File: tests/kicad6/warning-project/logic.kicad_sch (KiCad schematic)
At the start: 2 parts

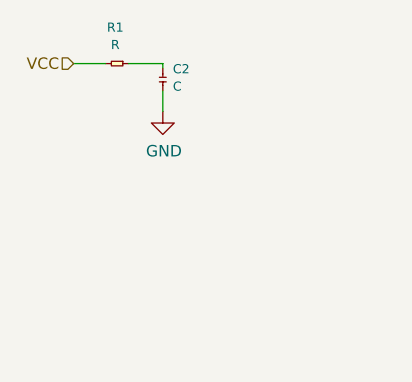
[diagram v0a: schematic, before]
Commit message: Changed the "warning" KiCad 6 schematic.
To report a warning, KiCad 6 ignores the previous.
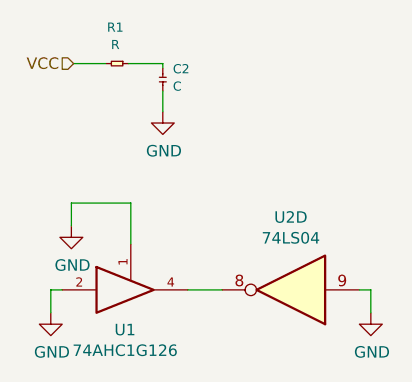
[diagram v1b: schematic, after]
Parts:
- added U1: 74AHC1G126, symbol 74xGxx:74AHC1G126
- added U2: 74LS04, symbol 74xx:74LS04
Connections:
- net GND: now also U1.1, U1.2, U1.3 (GND), U2.9
- net VCC: now also U1.5 (VCC)
- new net: U1.4, U2.8
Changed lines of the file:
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@@
   (page 3 3)
   (paper "A4")
+  (wire (pts (xy 132.334 96.012) (xy 132.334 98.552))
+    (stroke (width 0) (type solid) (color 0 0 0 0))
+  )
+  (wire (pts (xy 133.604 96.012) (xy 132.334 96.012))
+    (stroke (width 0) (type solid) (color 0 0 0 0))
+  )
+  (wire (pts (xy 134.62 86.36) (xy 141.224 86.36))
+    (stroke (width 0) (type solid) (color 0 0 0 0))
+  )
+  (wire (pts (xy 134.62 88.9) (xy 134.62 86.36))
+    (stroke (width 0) (type solid) (color 0 0 0 0))
+  )
   (wire (pts (xy 138.43 70.866) (xy 134.874 70.866))
     (stroke (width 0) (type solid) (color 0 0 0 0))
@@
     (stroke (width 0) (type solid) (color 0 0 0 0))
   )
+  (wire (pts (xy 141.224 86.36) (xy 141.224 90.932))
+    (stroke (width 0) (type solid) (color 0 0 0 0))
+  )
   (wire (pts (xy 144.78 70.866) (xy 144.78 71.374))
     (stroke (width 0) (type solid) (color 0 0 0 0))
   )
   (wire (pts (xy 144.78 73.914) (xy 144.78 76.2))
+    (stroke (width 0) (type solid) (color 0 0 0 0))
+  )
+  (wire (pts (xy 147.574 96.012) (xy 151.384 96.012))
+    (stroke (width 0) (type solid) (color 0 0 0 0))
+  )
+  (wire (pts (xy 166.624 96.012) (xy 167.894 96.012))
+    (stroke (width 0) (type solid) (color 0 0 0 0))
+  )
+  (wire (pts (xy 167.894 96.012) (xy 167.894 98.552))
     (stroke (width 0) (type solid) (color 0 0 0 0))
   )
@@
     )
   )
+  (symbol (lib_id "power:GND") (at 132.334 98.552 0) (unit 1)
+    (in_bom yes) (on_board yes)
+    (property "Reference" "#PWR04" (id 0) (at 132.334 104.902 0)
+      (effects (font (size 1.27 1.27)) hide)
+    )
+    (property "Value" "GND" (id 1) (at 132.461 102.9462 0))
+    (property "Footprint" "" (id 2) (at 132.334 98.552 0)
+      (effects (font (size 1.27 1.27)) hide)
+    )
+    (property "Datasheet" "" (id 3) (at 132.334 98.552 0)
+      (effects (font (size 1.27 1.27)) hide)
+    )
+  )
+  (symbol (lib_id "power:GND") (at 134.62 88.9 0) (unit 1)
+    (in_bom yes) (on_board yes)
+    (property "Reference" "#PWR05" (id 0) (at 134.62 95.25 0)
+      (effects (font (size 1.27 1.27)) hide)
+    )
+    (property "Value" "GND" (id 1) (at 134.747 93.2942 0))
+    (property "Footprint" "" (id 2) (at 134.62 88.9 0)
+      (effects (font (size 1.27 1.27)) hide)
+    )
+    (property "Datasheet" "" (id 3) (at 134.62 88.9 0)
+      (effects (font (size 1.27 1.27)) hide)
+    )
+  )
   (symbol (lib_id "power:GND") (at 144.78 76.2 0) (unit 1)
     (in_bom yes) (on_board yes)
@@
     (property "Datasheet" "" (id 3) (at 144.78 76.2 0))
   )
+  (symbol (lib_id "power:GND") (at 167.894 98.552 0) (unit 1)
+    (in_bom yes) (on_board yes)
+    (property "Reference" "#PWR06" (id 0) (at 167.894 104.902 0)
+      (effects (font (size 1.27 1.27)) hide)
+    )
+    (property "Value" "GND" (id 1) (at 168.021 102.9462 0))
+    (property "Footprint" "" (id 2) (at 167.894 98.552 0)
+      (effects (font (size 1.27 1.27)) hide)
+    )
+    (property "Datasheet" "" (id 3) (at 167.894 98.552 0)
+      (effects (font (size 1.27 1.27)) hide)
+    )
+  )
+  (symbol (lib_id "74xGxx:74AHC1G126") (at 141.224 96.012 0) (unit 1)
+    (in_bom yes) (on_board yes)
+    (property "Reference" "U1" (id 0) (at 140.589 100.4634 0))
+    (property "Value" "74AHC1G126" (id 1) (at 140.589 102.7621 0))
+    (property "Footprint" "" (id 2) (at 141.224 96.012 0)
+      (effects (font (size 1.27 1.27)) hide)
+    )
+    (property "Datasheet" "http://www.ti.com/lit/sg/scyt129e/scyt129e.pdf" (id 3) (at 141.224 96.012 0)
+      (effects (font (size 1.27 1.27)) hide)
+    )
+  )
+  (symbol (lib_id "74xx:74LS04") (at 159.004 96.012 180) (unit 4)
+    (in_bom yes) (on_board yes)
+    (property "Reference" "U2" (id 0) (at 159.004 87.9602 0))
+    (property "Value" "74LS04" (id 1) (at 159.004 90.2716 0))
+    (property "Footprint" "" (id 2) (at 159.004 96.012 0)
+      (effects (font (size 1.27 1.27)) hide)
+    )
+    (property "Datasheet" "http://www.ti.com/lit/gpn/sn74LS04" (id 3) (at 159.004 96.012 0)
+      (effects (font (size 1.27 1.27)) hide)
+    )
+  )
 )
